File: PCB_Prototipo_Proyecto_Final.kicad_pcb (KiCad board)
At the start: 2 copper layers, 165.1 x 164.9 mm, 158 parts, among them IC1 UA741CP, J1 VIN, J10 Terminal_Sensores_Nivel, J11 Terminal_Sensor_Flujo, J12 Rele_4, J13 Rele_7, J14 Rele_1, J15 Rele_5, J16 Rele_2, J17 Rele_3, J18 Rele_6, J19 Pin_3V3, J2 Conn_01x15, J20 Conector 3V3, J21 Conector GND, J22 Pin_3V3, J23 Pin_3V3, J24 Pin GND, J25 Pin_3V3, J26 Pin GND, J27 Pin_3V3, J28 Pin_3V3, J29 Pin_3V3, J3 Conn_01x15, J30 Pin GND, J31 Pin GND, J32 Pin GND, J33 Pin GND, J34 Pin GND, J35 Pin GND, J36 Pin GND, J37 Pin GND, J38 Pin GND, J39 Pin GND, J4 Terminal_Sensor_pH, J40 Pin GND, J41 Pin GND, J42 Pin GND, J43 Conector GND, J44 Pin GND, J45 Pin_3V3, J46 Pin GND, J47 Pin GND, J5 Terminal_Sensor_CO2, J6 Terminal_Sensor_TDS, J7 Terminal_Sensor_Temp_Sumerg, J8 Terminal_Sensor_Iluminacion, J9 Terminal_Sensor_Temp_y_Hum, K1 SRD-05VDC-SL-C, K2 SRD-05VDC-SL-C, K3 SRD-05VDC-SL-C, K4 SRD-05VDC-SL-C, K5 SRD-05VDC-SL-C, K6 SRD-05VDC-SL-C, K7 SRD-05VDC-SL-C, Q1 2N7002, Q10 2N7002, Q11 2N7002, Q12 2N7002, Q13 2N7002, Q14 2N7002, Q15 2N7002, Q2 2N7002, Q3 2N7002, Q4 2N7002, Q5 2N7002, Q6 2N7002, Q7 2N7002, Q8 2N7002, Q9 2N7002, U1 LM2596S-ADJ, U2 LM1117-3.3, U3 MCP23008-xP

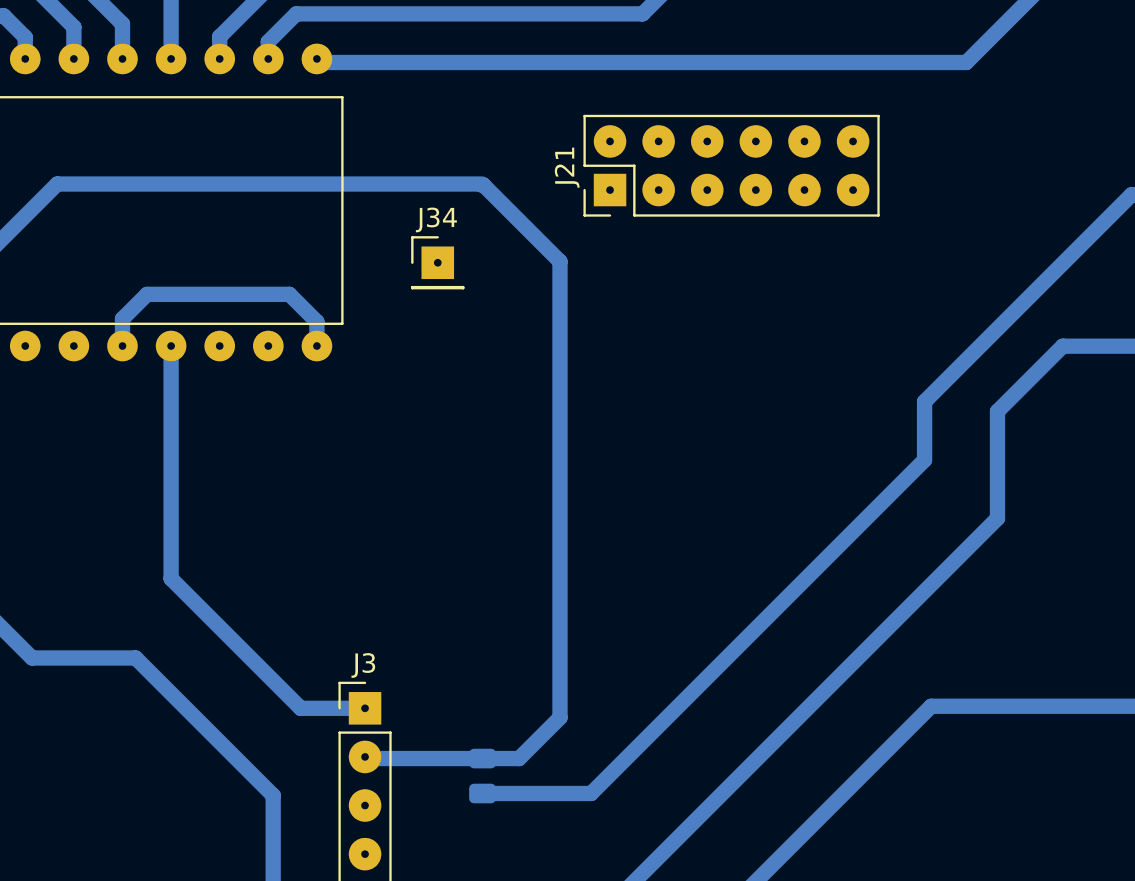
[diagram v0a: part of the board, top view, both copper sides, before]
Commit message: Corrección de errores menores y generación de Gerbers.
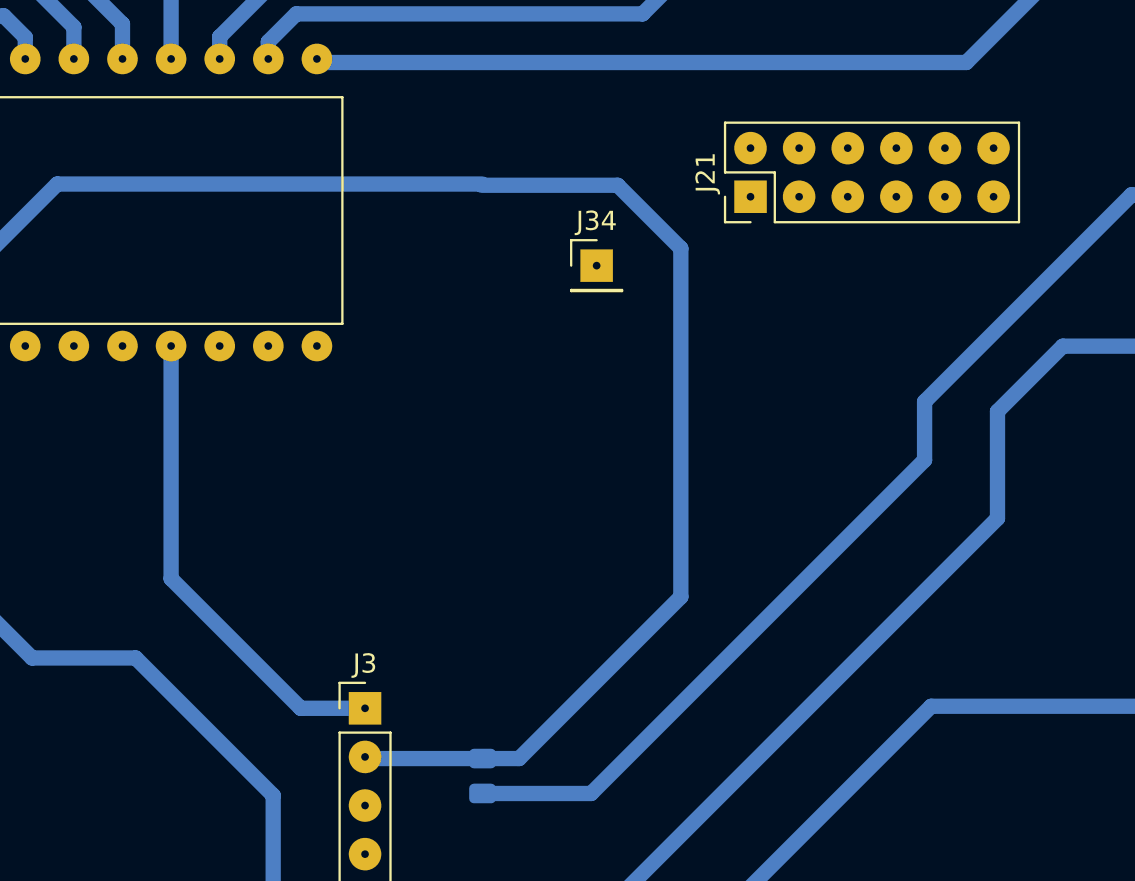
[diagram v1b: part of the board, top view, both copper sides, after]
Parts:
- moved J34 8.30 mm to (240.4, 103.4)
- moved J21 7.35 mm to (248.5, 99.8)
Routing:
- net GND: track 14.0 -> 0.00 mm
- net /Microcontrolador/MCP23008_SCL: track 74.1 -> 83.5 mm
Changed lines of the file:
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@@
   )
   (footprint "Connector_PinHeader_2.54mm:PinHeader_1x01_P2.54mm_Vertical" (layer "F.Cu")
-    (at 232.120714 103.23)
+    (at 240.420714 103.38)
     (descr "Through hole straight pin header, 1x01, 2.54mm pitch, single row")
     (tags "Through hole pin header THT 1x01 2.54mm single row")
@@
   )
   (footprint "Connector_PinHeader_2.54mm:PinHeader_2x06_P2.54mm_Vertical" (layer "F.Cu")
-    (at 241.120714 99.43 90)
+    (at 248.460714 99.78 90)
     (descr "Through hole straight pin header, 2x06, 2.54mm pitch, double rows")
     (tags "Through hole pin header THT 2x06 2.54mm double row")
@@
   (segment (start 216.05 191.65) (end 216.05 188.65) (width 0.8) (layer "B.Cu") (net 1))
   (segment (start 216.05 188.65) (end 216.05 185.05) (width 0.8) (layer "B.Cu") (net 1))
-  (segment (start 216.929714 104.88) (end 224.370714 104.88) (width 0.8) (layer "B.Cu") (net 2))
-  (segment (start 215.646 107.58) (end 215.646 106.163714) (width 0.8) (layer "B.Cu") (net 2))
-  (segment (start 215.646 106.163714) (end 216.929714 104.88) (width 0.8) (layer "B.Cu") (net 2))
-  (segment (start 225.806 106.315286) (end 225.806 107.58) (width 0.8) (layer "B.Cu") (net 2))
-  (segment (start 224.370714 104.88) (end 225.806 106.315286) (width 0.8) (layer "B.Cu") (net 2))
   (segment (start 201.25 188.05) (end 201.15 188.15) (width 0.8) (layer "B.Cu") (net 3))
   (segment (start 201.15 191.5375) (end 201.15 188.15) (width 0.8) (layer "B.Cu") (net 3))
@@
   (segment (start 218.186 119.735585) (end 224.960415 126.51) (width 0.8) (layer "B.Cu") (net 37))
   (segment (start 218.186 107.58) (end 218.186 119.735585) (width 0.8) (layer "B.Cu") (net 37))
-  (segment (start 234.520714 99.18) (end 238.506 103.165286) (width 0.8) (layer "B.Cu") (net 38))
-  (segment (start 228.4055 129.1355) (end 228.32 129.05) (width 0.8) (layer "B.Cu") (net 38))
   (segment (start 212.234714 99.116) (end 234.442 99.116) (width 0.8) (layer "B.Cu") (net 38))
-  (segment (start 234.420714 99.18) (end 234.520714 99.18) (width 0.8) (layer "B.Cu") (net 38))
-  (segment (start 238.506 127) (end 236.3705 129.1355) (width 0.8) (layer "B.Cu") (net 38))
-  (segment (start 238.506 103.165286) (end 238.506 127) (width 0.8) (layer "B.Cu") (net 38))
   (segment (start 236.3705 129.1355) (end 228.4055 129.1355) (width 0.8) (layer "B.Cu") (net 38))
+  (segment (start 234.420714 99.18) (end 241.520714 99.18) (width 0.8) (layer "B.Cu") (net 38))
+  (segment (start 244.820714 120.685286) (end 236.3705 129.1355) (width 0.8) (layer "B.Cu") (net 38))
+  (segment (start 241.520714 99.18) (end 244.820714 102.48) (width 0.8) (layer "B.Cu") (net 38))
+  (segment (start 244.820714 102.48) (end 244.820714 120.685286) (width 0.8) (layer "B.Cu") (net 38))
   (segment (start 205.486 105.864714) (end 212.234714 99.116) (width 0.8) (layer "B.Cu") (net 38))
+  (segment (start 228.4055 129.1355) (end 228.32 129.05) (width 0.8) (layer "B.Cu") (net 38))
   (segment (start 205.486 107.58) (end 205.486 105.864714) (width 0.8) (layer "B.Cu") (net 38))
   (segment (start 216.336 123.88) (end 210.920714 123.88) (width 0.8) (layer "B.Cu") (net 41))
